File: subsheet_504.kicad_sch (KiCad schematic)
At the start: 36 parts, among them J502 Phono LEFT, J503 Phono RIGHT, U504 LF347N_mu, U508 LMC1992CCN_PHY

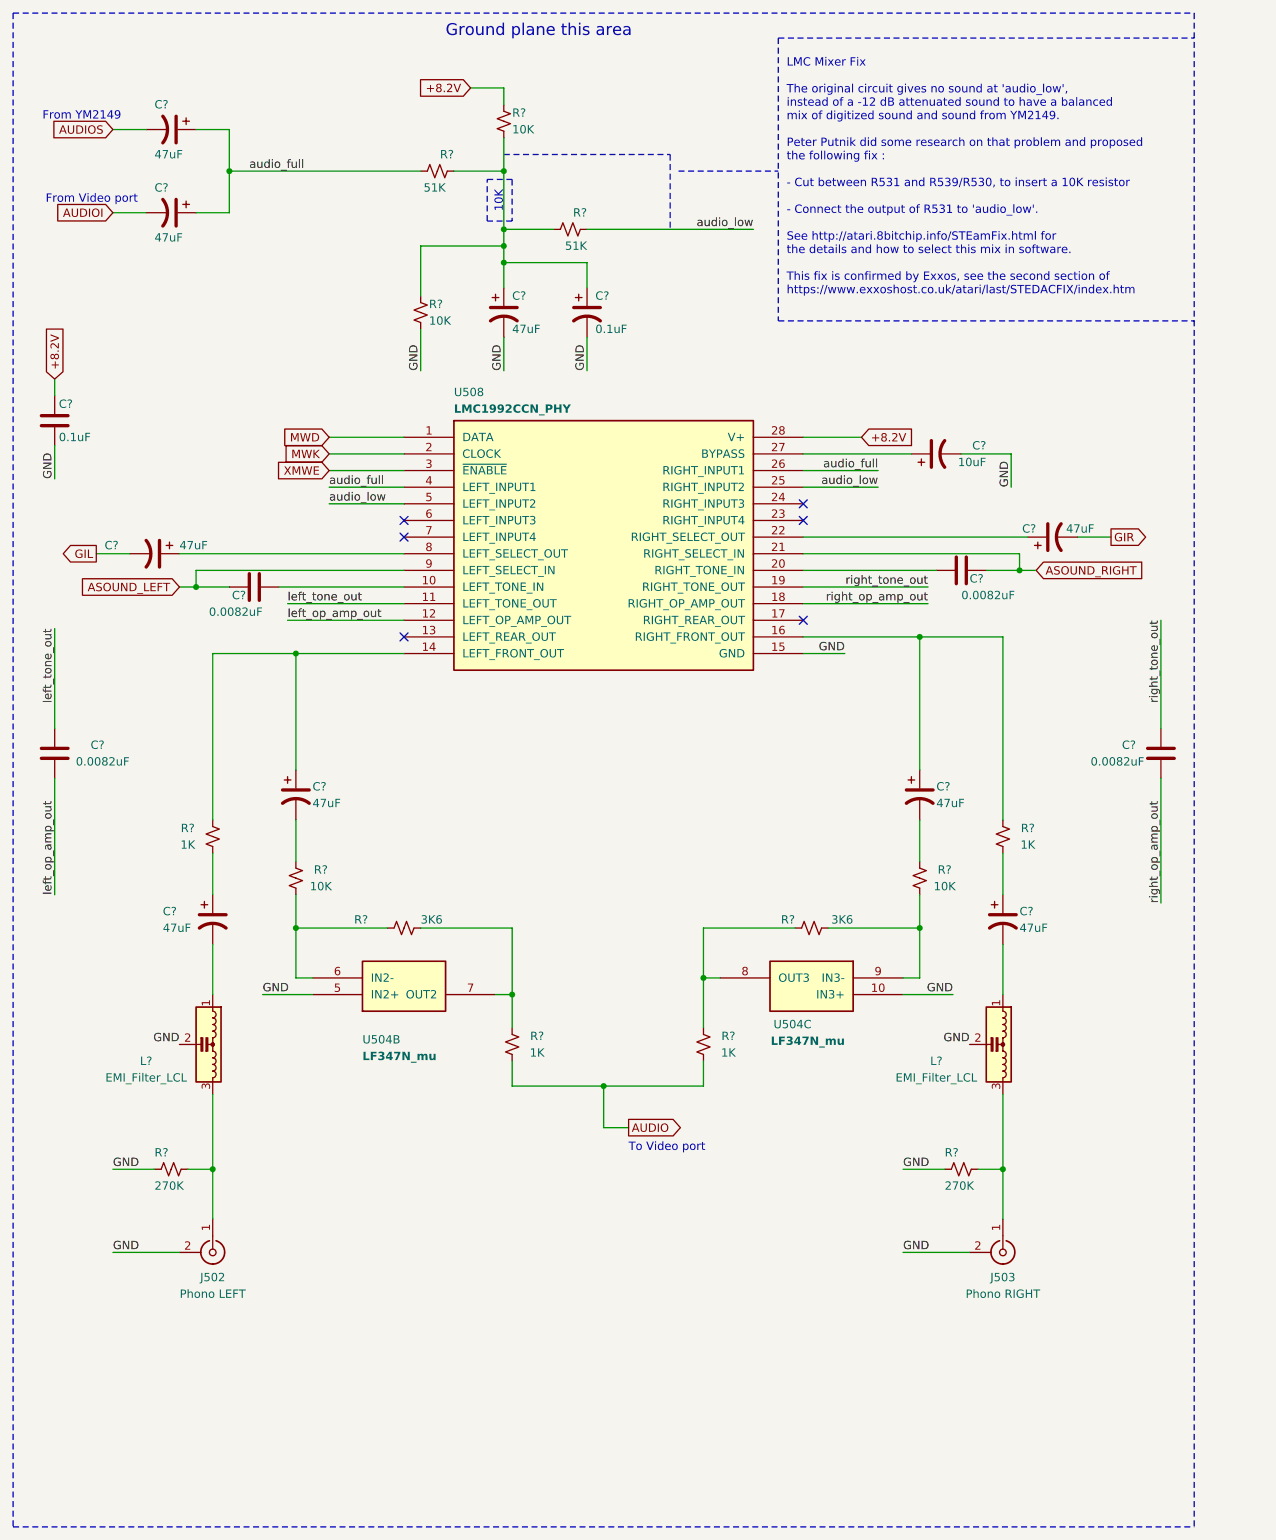
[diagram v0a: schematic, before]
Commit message: Resolves #3 : [schematic] annotate video port with signal name
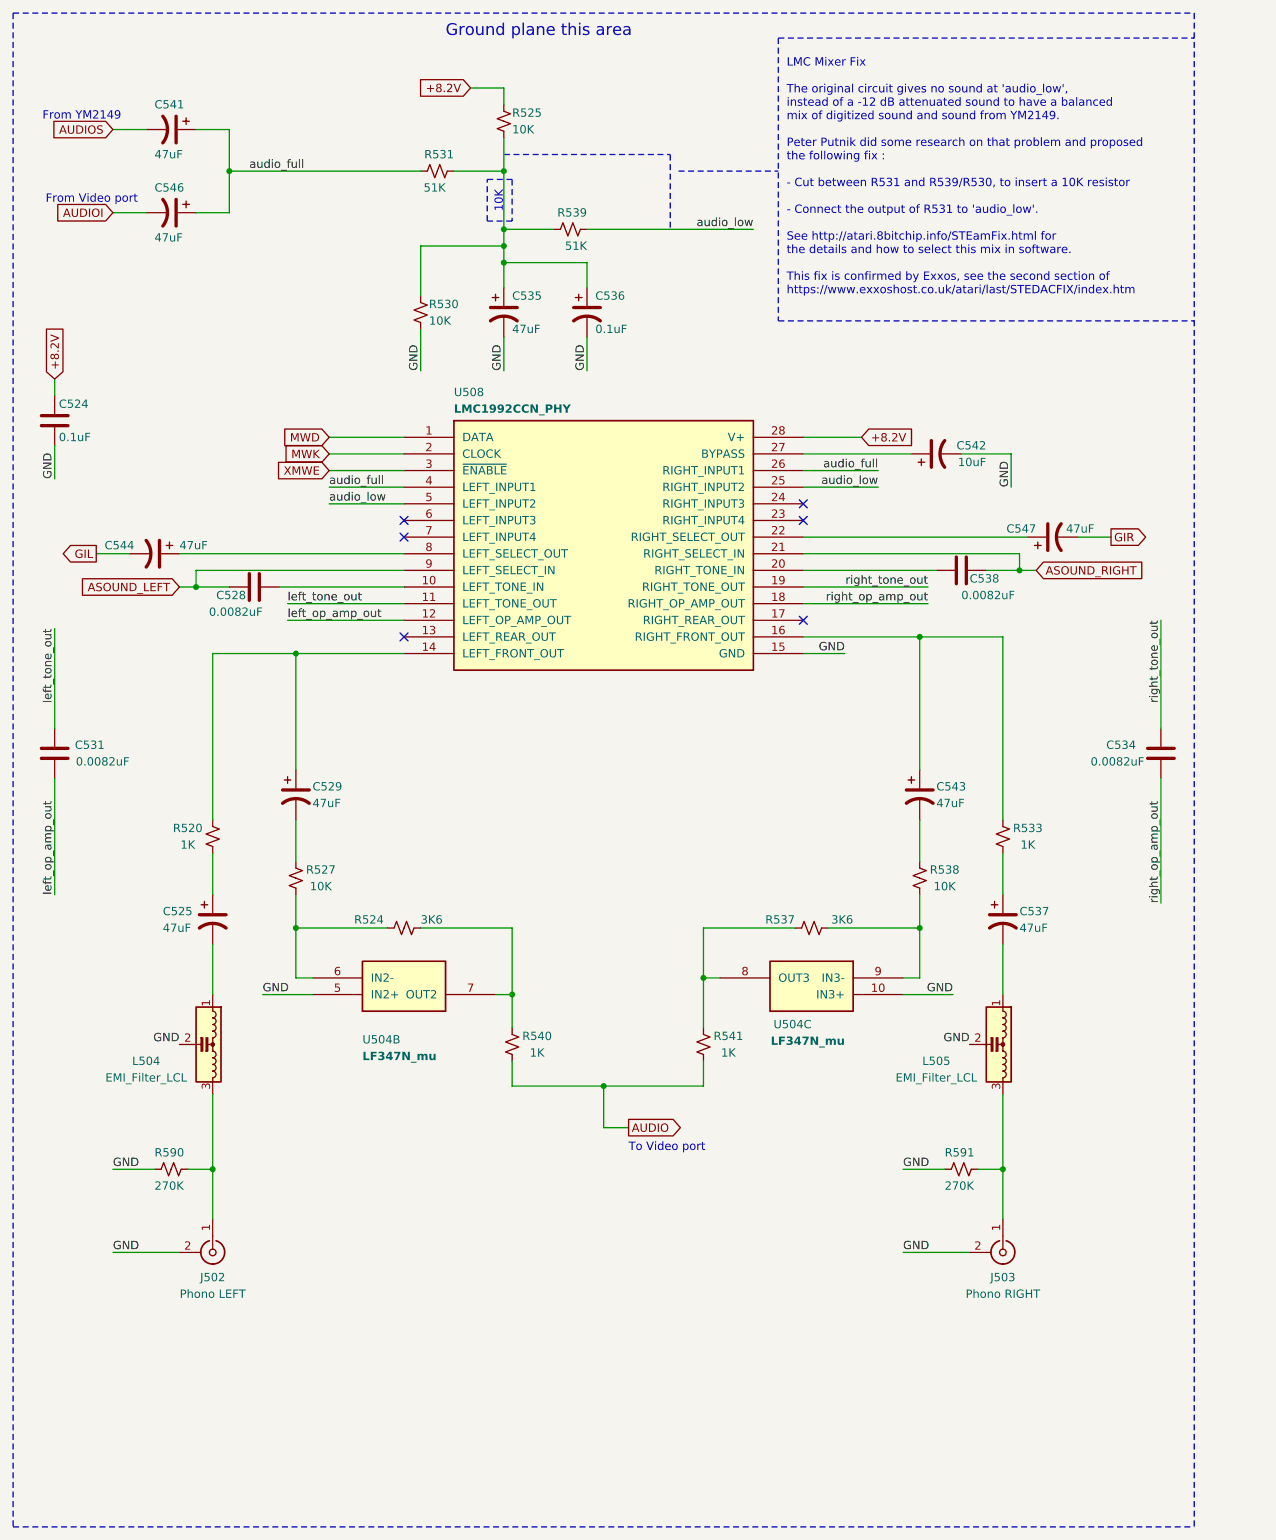
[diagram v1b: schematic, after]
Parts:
- gave numbers to parts that had none: 32
